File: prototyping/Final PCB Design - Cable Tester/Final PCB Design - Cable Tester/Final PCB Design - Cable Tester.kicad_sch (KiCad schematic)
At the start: 41 parts, among them J17 Banana Jack, J20 SFML-110-02-L-D-A, J3 Debug Connection, J4 MEM2061-01-188-00-A_REVA, J5 Barrel Jack 9V, J6 Touchscreen HMI, Q1 2N3904, SW1 Rocker Switch, U1 AVR128DB64x-xMR, U2 LP2985-3.3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

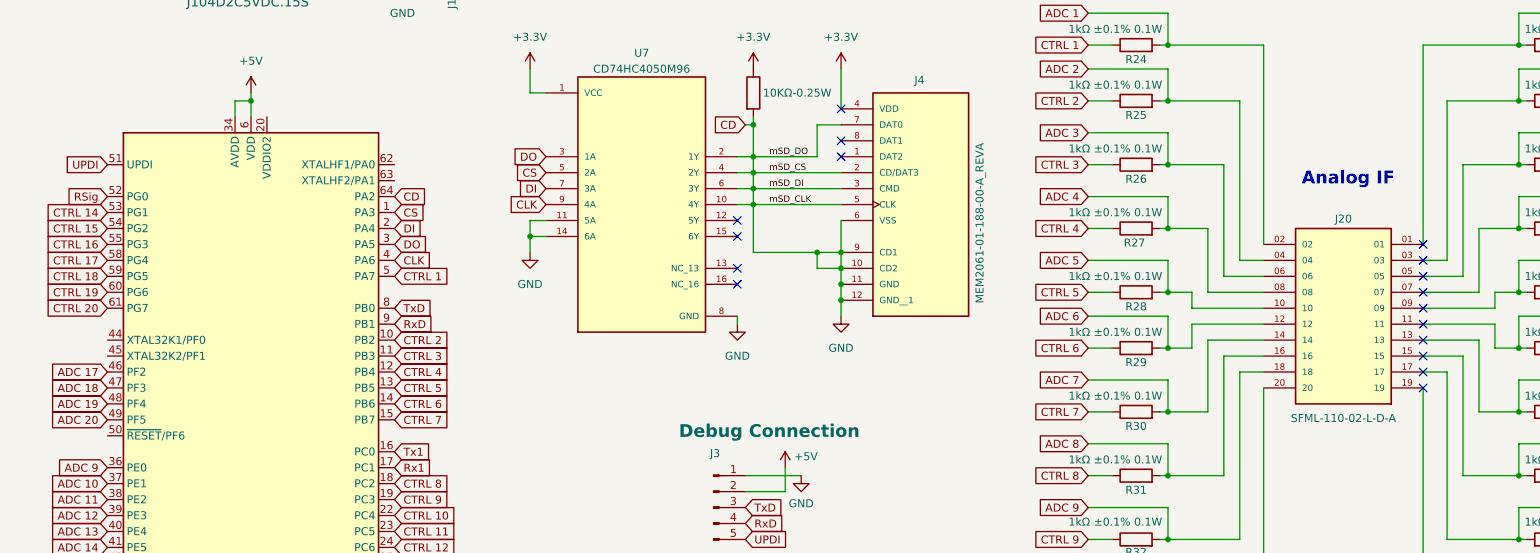
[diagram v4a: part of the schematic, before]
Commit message: Laying out final PCB.
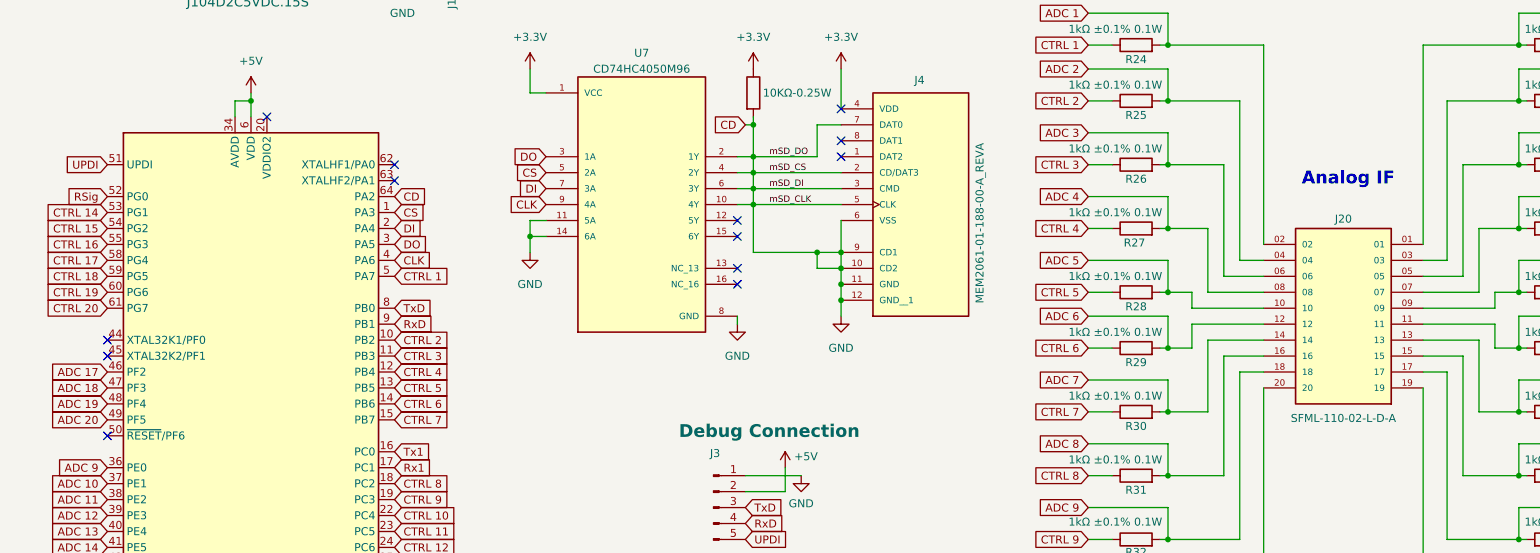
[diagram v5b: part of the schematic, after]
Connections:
- no-connect marks 20 -> 16
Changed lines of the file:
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@@
+	)
+	(no_connect
+		(at 80.01 92.71)
+	)
+	(no_connect
+		(at 34.29 120.65)
 	)
 	(no_connect
@@
 	)
 	(no_connect
-		(at 243.84 125.73)
+		(at 59.69 82.55)
 	)
 	(no_connect
@@
 	)
 	(no_connect
-		(at 151.13 81.28)
+		(at 80.01 90.17)
 	)
 	(no_connect
-		(at 243.84 115.57)
+		(at 151.13 81.28)
 	)
 	(no_connect
@@
 	)
 	(no_connect
-		(at 243.84 102.87)
-	)
-	(no_connect
 		(at 134.62 109.22)
-	)
-	(no_connect
-		(at 243.84 123.19)
-	)
-	(no_connect
-		(at 243.84 120.65)
 	)
 	(no_connect
@@
 	)
 	(no_connect
-		(at 243.84 105.41)
-	)
-	(no_connect
 		(at 36.83 59.69)
 	)
 	(no_connect
-		(at 243.84 113.03)
+		(at 34.29 118.11)
 	)
 	(no_connect
-		(at 243.84 107.95)
-	)
-	(no_connect
-		(at 243.84 110.49)
-	)
-	(no_connect
-		(at 243.84 118.11)
+		(at 34.29 133.35)
 	)
 	(wire

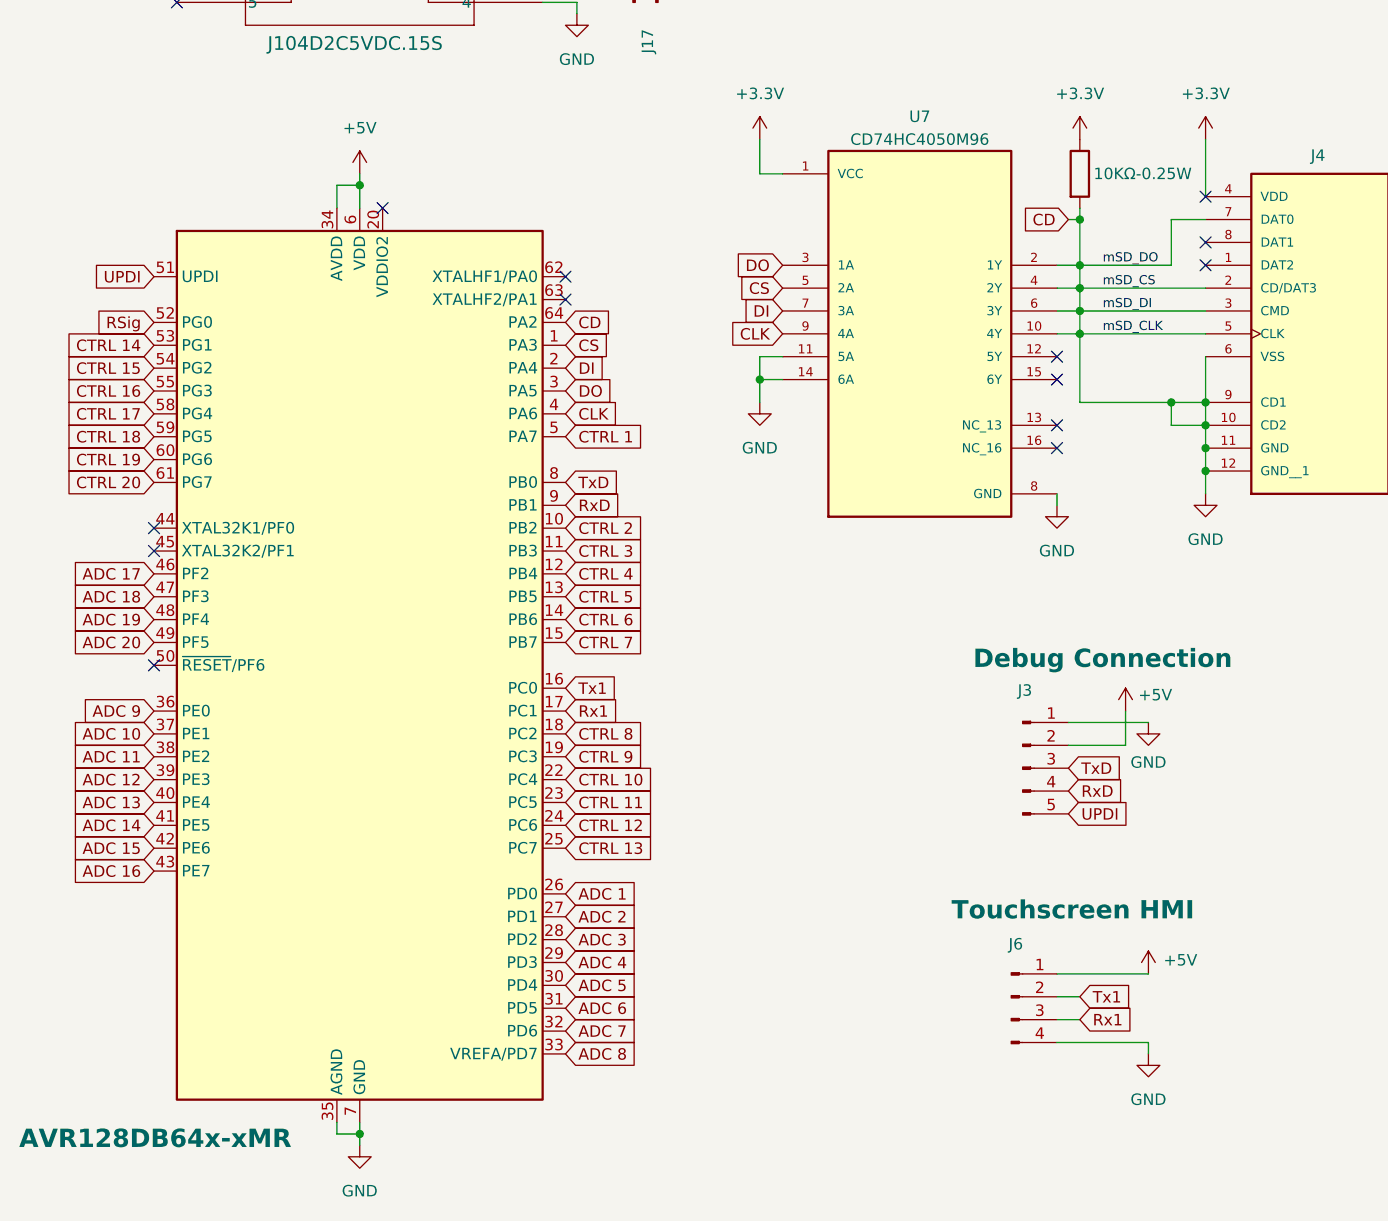
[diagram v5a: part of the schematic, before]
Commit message: Updates to final PCB
Final PCB design updates - placed traces and vias to Analog IF circuit and changed order of analog pins 1-10 on schematic and PCB layout.
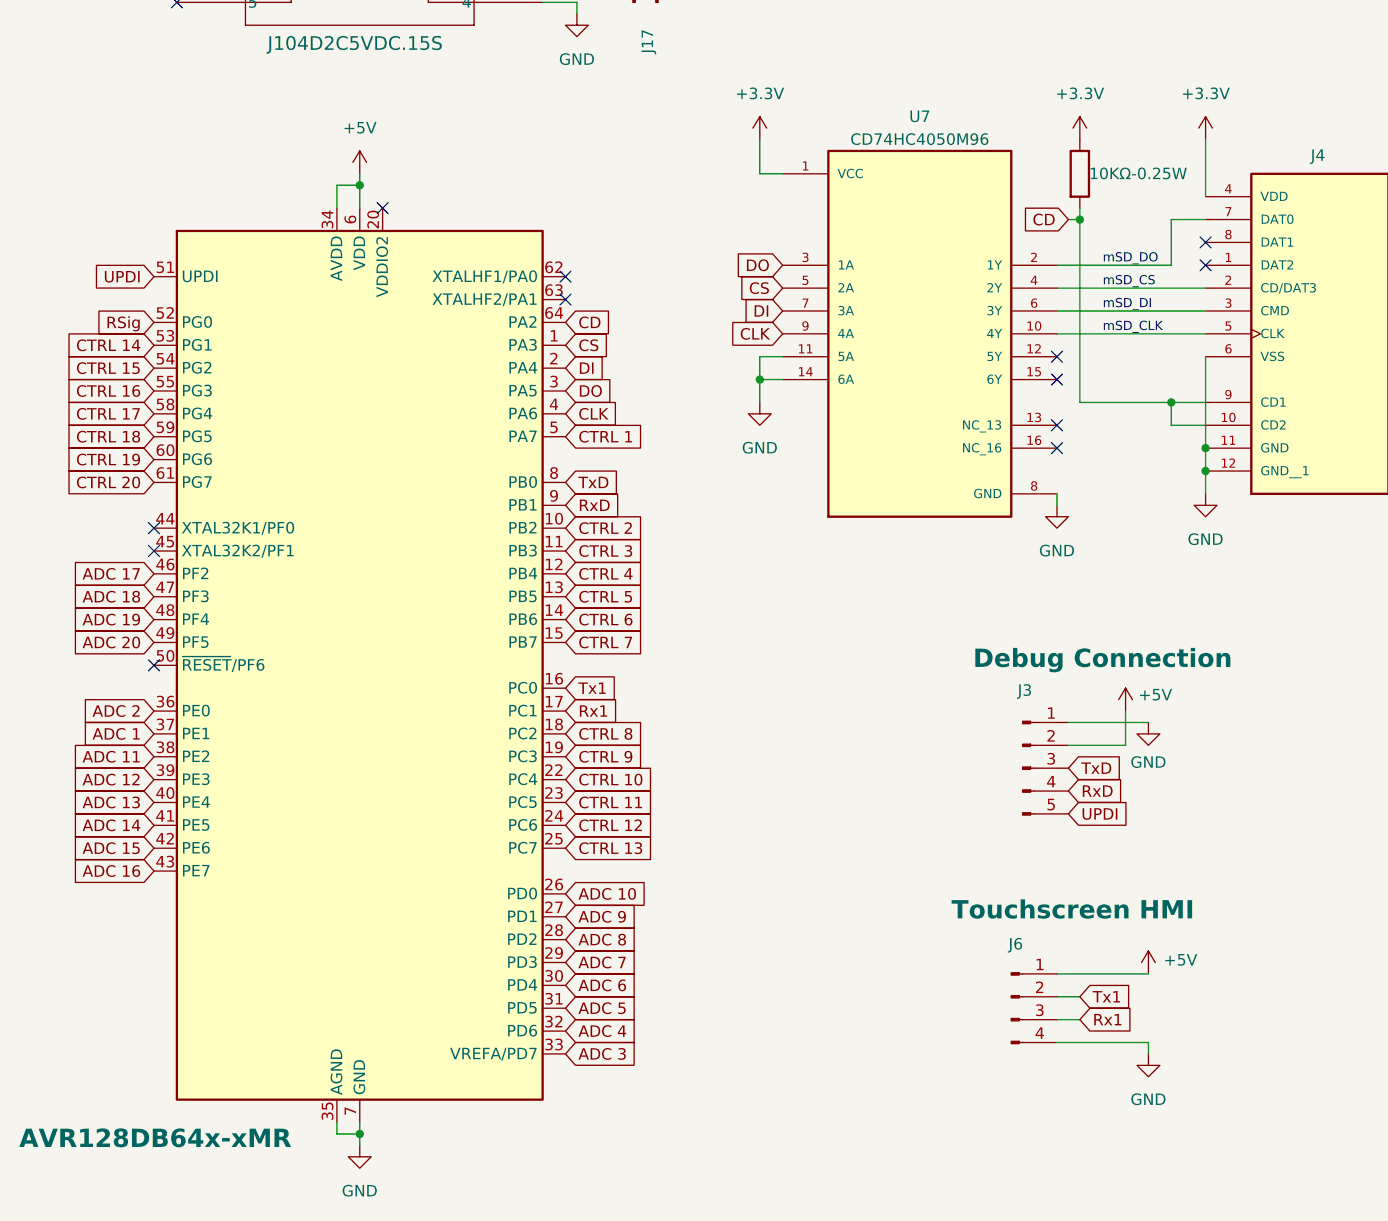
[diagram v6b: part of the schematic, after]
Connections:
- net ADC 1: now also U1.37 (PE1); no longer U1.26 (PD0)
- net ADC 10: now also U1.26 (PD0); no longer U1.37 (PE1)
- net ADC 2: now also U1.36 (PE0); no longer U1.27 (PD1)
- net ADC 3: now also U1.33 (VREFA/PD7); no longer U1.28 (PD2)
- net ADC 4: now also U1.32 (PD6); no longer U1.29 (PD3)
- net ADC 5: now also U1.31 (PD5); no longer U1.30 (PD4)
- net ADC 6: now also U1.30 (PD4); no longer U1.31 (PD5)
- net ADC 7: now also U1.29 (PD3); no longer U1.32 (PD6)
- net ADC 8: now also U1.28 (PD2); no longer U1.33 (VREFA/PD7)
- net ADC 9: now also U1.27 (PD1); no longer U1.36 (PE0)
- net GND: no longer J4.10 (CD2), J4.2 (CD/DAT3), J4.3 (CMD), J4.5 (CLK), J4.7 (DAT0), J4.9 (CD1), R2.2, U1.64 (PA2), U7.10 (4Y), U7.2 (1Y), U7.4 (2Y), U7.6 (3Y)
- new net CD: J4.10 (CD2), J4.9 (CD1), R2.2, U1.64 (PA2)
- new net mSD_CLK: J4.5 (CLK), U7.10 (4Y)
- new net mSD_CS: J4.2 (CD/DAT3), U7.4 (2Y)
- new net mSD_DI: J4.3 (CMD), U7.6 (3Y)
- new net mSD_DO: J4.7 (DAT0), U7.2 (1Y)
- no-connect marks 16 -> 15
